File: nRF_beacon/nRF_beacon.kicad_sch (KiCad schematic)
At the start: 11 parts, among them J1 Conn_02x05_Odd_Even, J2 Conn_02x03_Counter_Clockwise, U4 12BHC186P1-GR

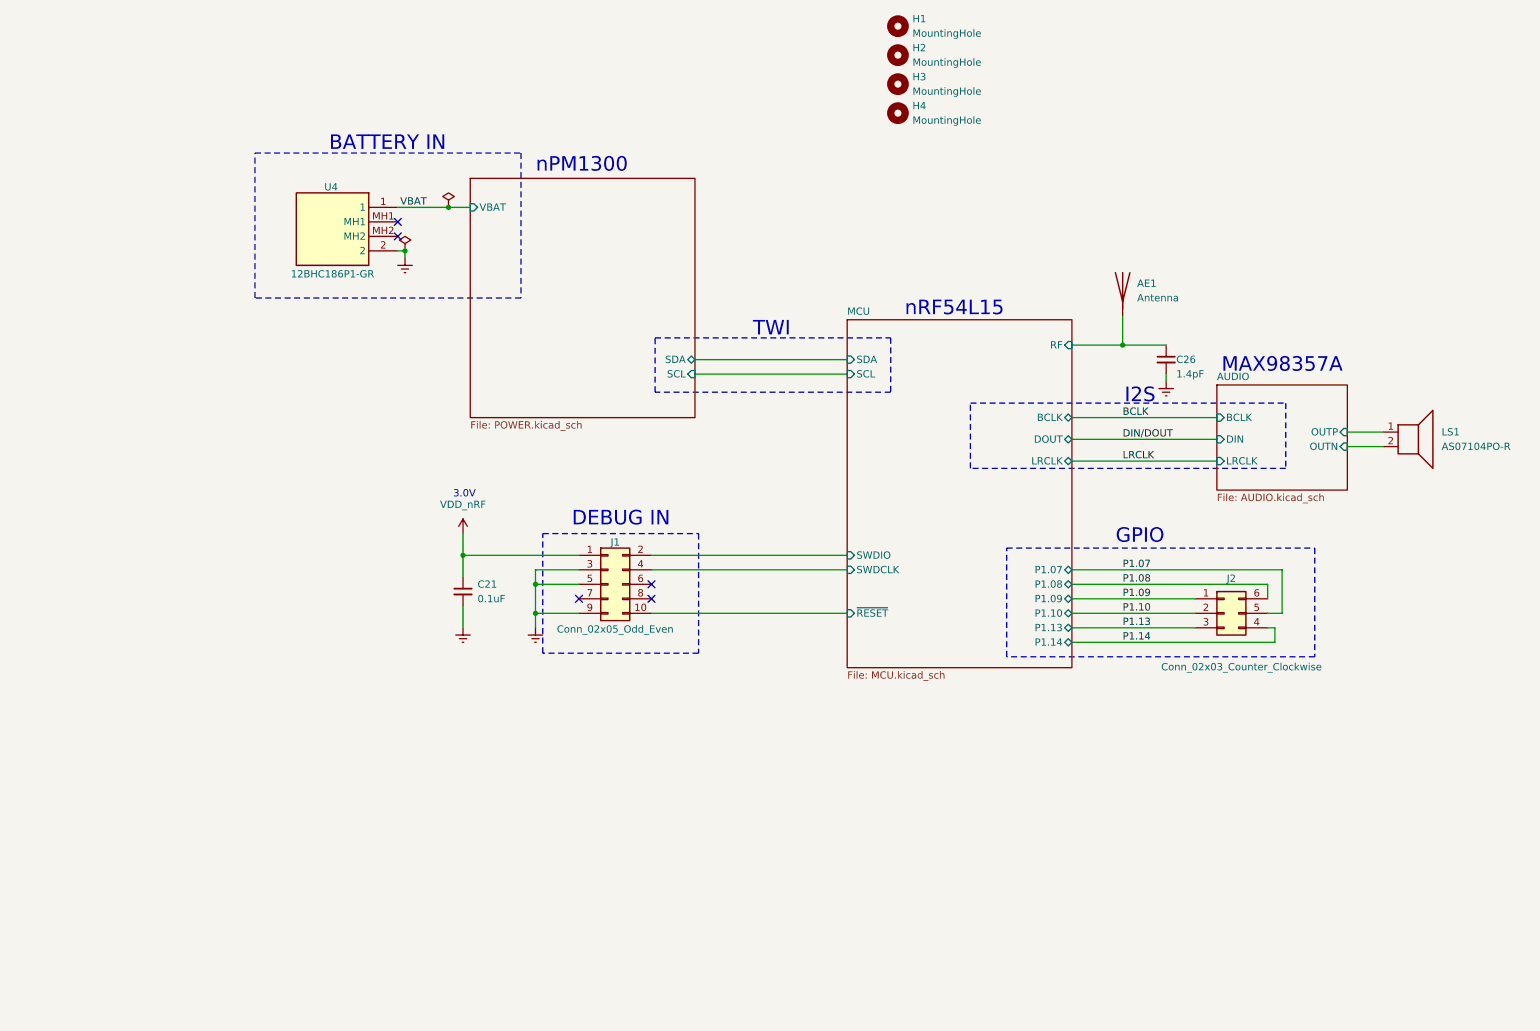
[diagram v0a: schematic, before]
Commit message: Adjustments to GPIO connector. Added testpads. Polygon pour by antenna for correct impedance matching
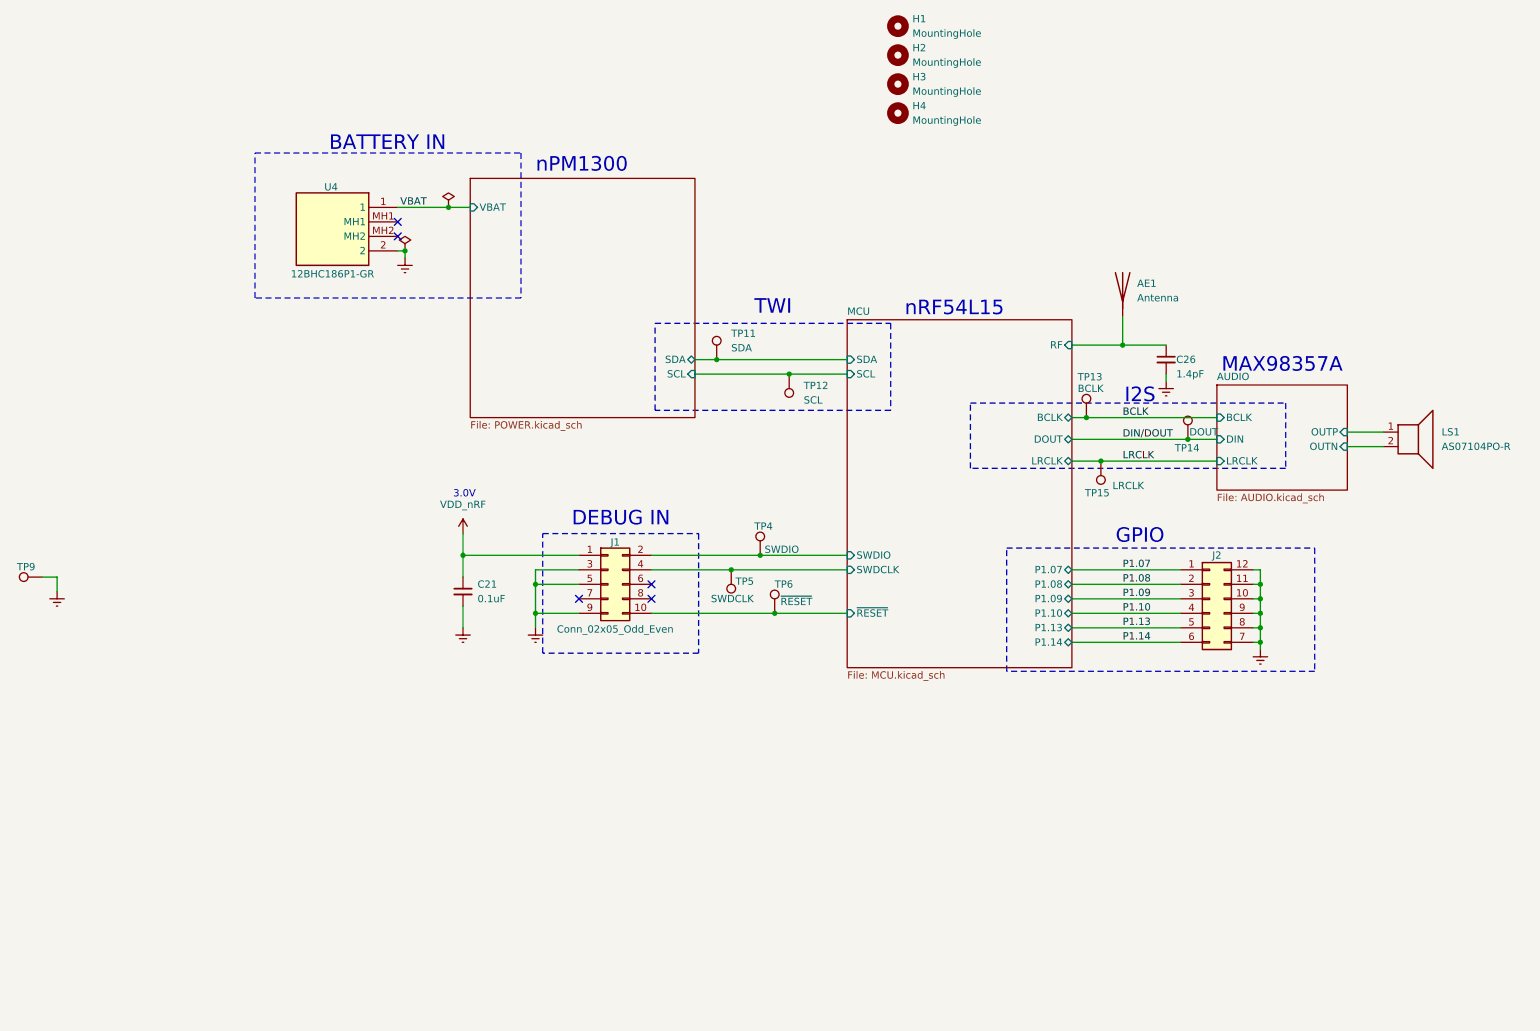
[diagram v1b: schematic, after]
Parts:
- added TP11: SDA, TestPoint:TestPoint_Pad_D1.0mm, symbol Connector:TestPoint
- added TP12: SCL, TestPoint:TestPoint_Pad_D1.0mm, symbol Connector:TestPoint
- added TP13: BCLK, TestPoint:TestPoint_Pad_D1.0mm, symbol Connector:TestPoint
- added TP14: DOUT, TestPoint:TestPoint_Pad_D1.0mm, symbol Connector:TestPoint
- added TP15: LRCLK, TestPoint:TestPoint_Pad_D1.0mm, symbol Connector:TestPoint
- added TP4: SWDIO, TestPoint:TestPoint_Pad_D1.0mm, symbol Connector:TestPoint
- added TP5: SWDCLK, TestPoint:TestPoint_Pad_D1.0mm, symbol Connector:TestPoint
- added TP6: ~{RESET}, TestPoint:TestPoint_Pad_D1.0mm, symbol Connector:TestPoint
- added TP9: GND, TestPoint:TestPoint_Pad_D1.0mm, symbol Connector:TestPoint
- J2: footprint Ekse:SAMTEC_TSM-103-01-L-DV-P-TR -> Connector_PinHeader_2.54mm:PinHeader_2x06_P2.54mm_Vertical; symbol Connector_Generic:Conn_02x03_Counter_Clockwise -> Connector_Generic:Conn_02x06_Counter_Clockwise
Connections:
- net BCLK: now also TP13.1
- net DIN/DOUT: now also TP14.1
- net GND: now also J2.10 (Pin_10), J2.11 (Pin_11), J2.12 (Pin_12), J2.7 (Pin_7), J2.8 (Pin_8), J2.9 (Pin_9), TP9.1
- net LRCLK: now also TP15.1
- net MCU/SCL: now also TP12.1
- net MCU/SDA: now also TP11.1
- net MCU/SWDCLK: now also TP5.1
- net MCU/SWDIO: now also TP4.1
- net MCU/~{RESET}: now also TP6.1
- net P1.07: now also J2.1 (Pin_1); no longer J2.5 (Pin_5)
- net P1.08: now also J2.2 (Pin_2); no longer J2.6 (Pin_6)
- net P1.09: now also J2.3 (Pin_3); no longer J2.1 (Pin_1)
- net P1.10: now also J2.4 (Pin_4); no longer J2.2 (Pin_2)
- net P1.13: now also J2.5 (Pin_5); no longer J2.3 (Pin_3)
- net P1.14: now also J2.6 (Pin_6); no longer J2.4 (Pin_4)

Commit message: Added stitching vias and completed DRC tests
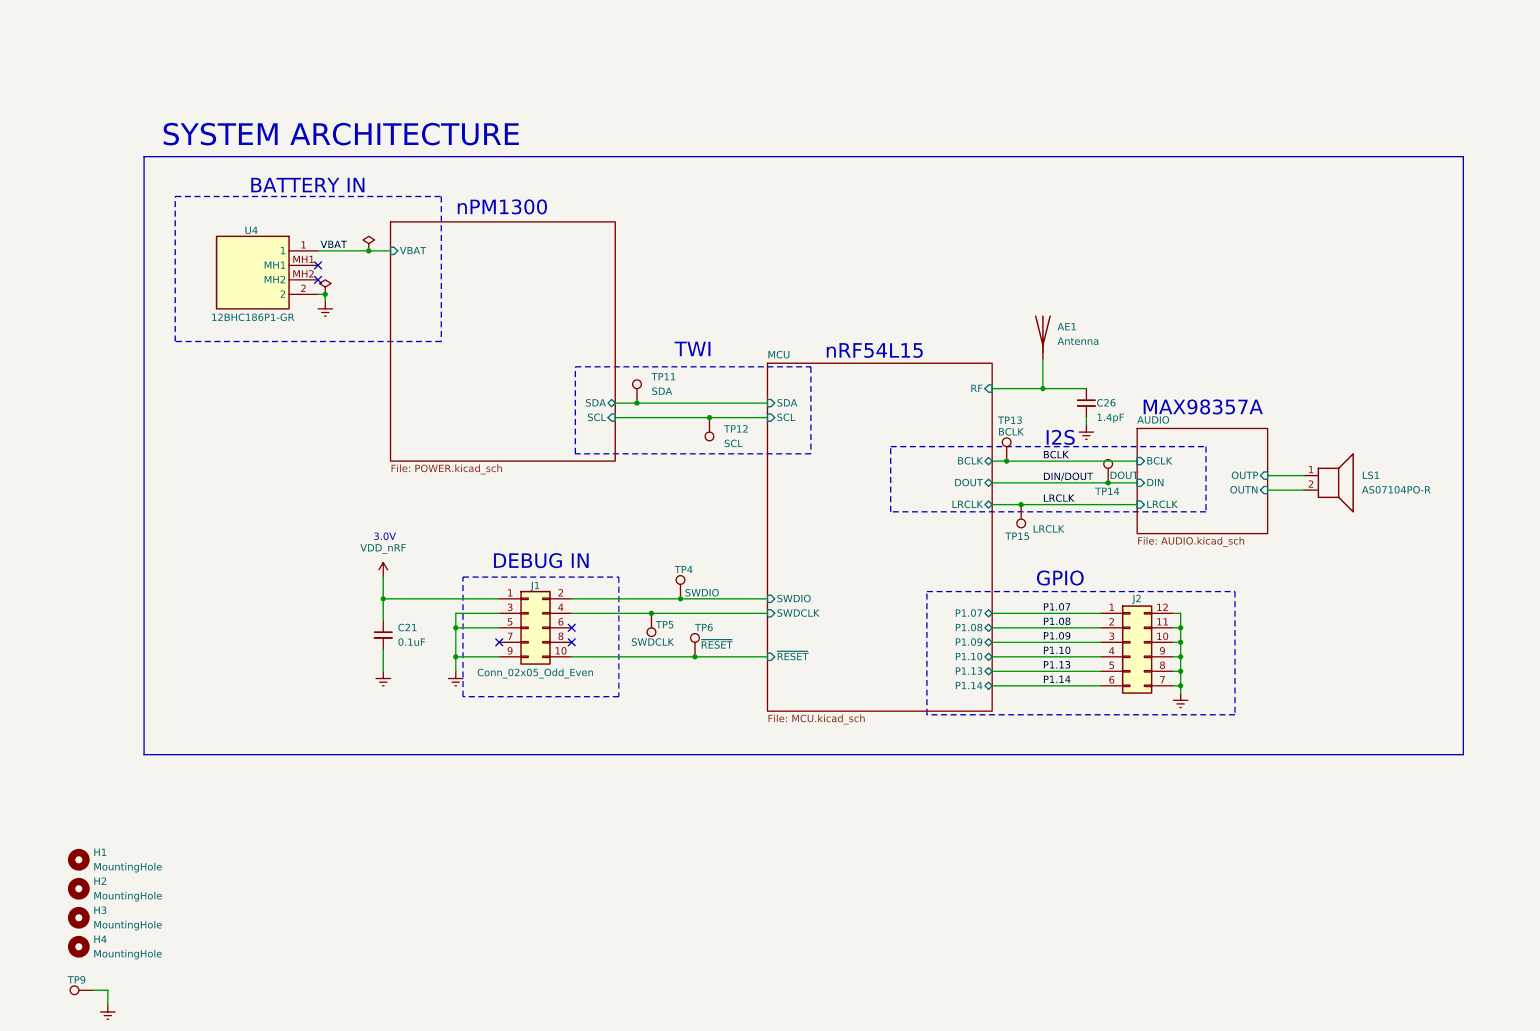
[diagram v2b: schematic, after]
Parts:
- AE1: now left out of the parts list
- C26: MPN (none) -> GCQ0335C1H1R4WB01D; Price (none) -> 1.8
- J2: MPN TSM-103-01-L-DV-P-TR -> (none); Price 9.48 -> (none)
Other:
- note added: "SYSTEM ARCHITECTURE"
- company: (none) -> Mathias Ekse
- title: (none) -> nRF54L15 BLE Sound Beacon
- moved on the sheet: AE1, C21, C26, H1, H2, H3, H4, J1, J2, LS1, TP11, TP12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

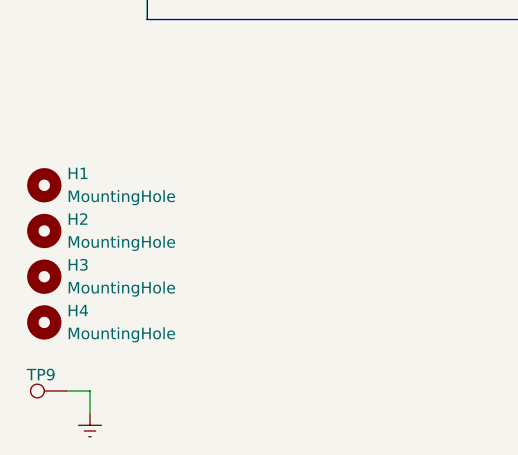
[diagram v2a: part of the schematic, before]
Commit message: Completed layout for Revision A (Prototype). Created gerber files
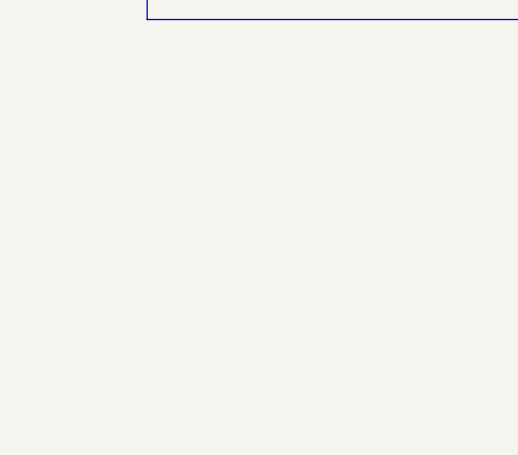
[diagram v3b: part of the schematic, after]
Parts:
- removed H1, H2, H3, H4: MountingHole, MountingHole:MountingHole_3.2mm_M3, symbol Mechanical:MountingHole
- removed TP9: GND, TestPoint:TestPoint_Pad_D1.0mm, symbol Connector:TestPoint
